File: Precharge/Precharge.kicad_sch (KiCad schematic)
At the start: 6 parts, among them J1 1053091202, J2 1053091203, J3 1053091202, K1 Relay_SPST-NO, K2 Relay_SPST-NO

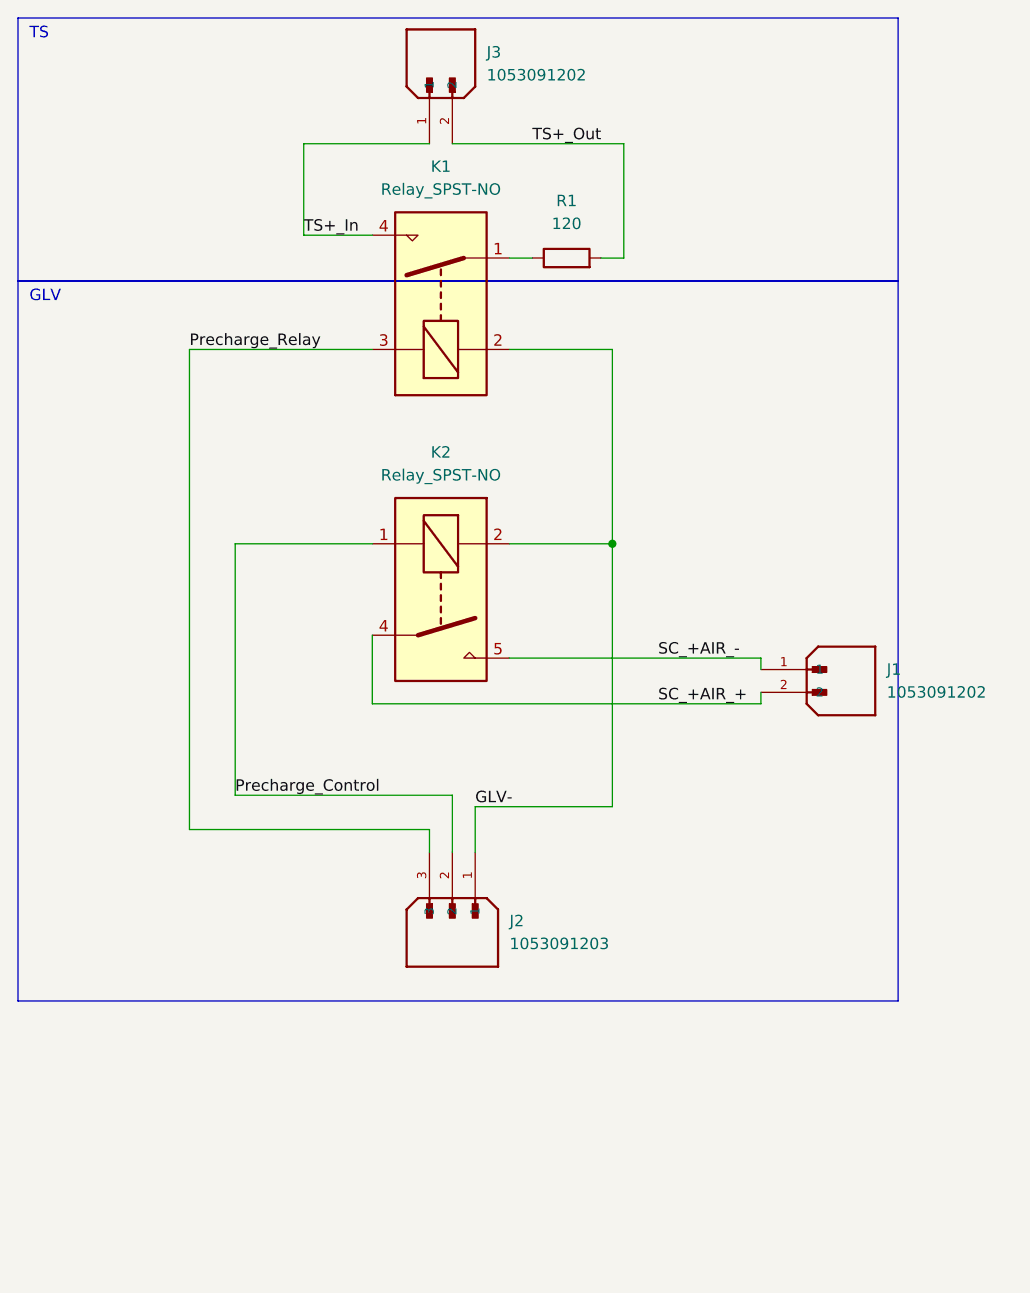
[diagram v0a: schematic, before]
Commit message: Added diodes to Precharge PCB
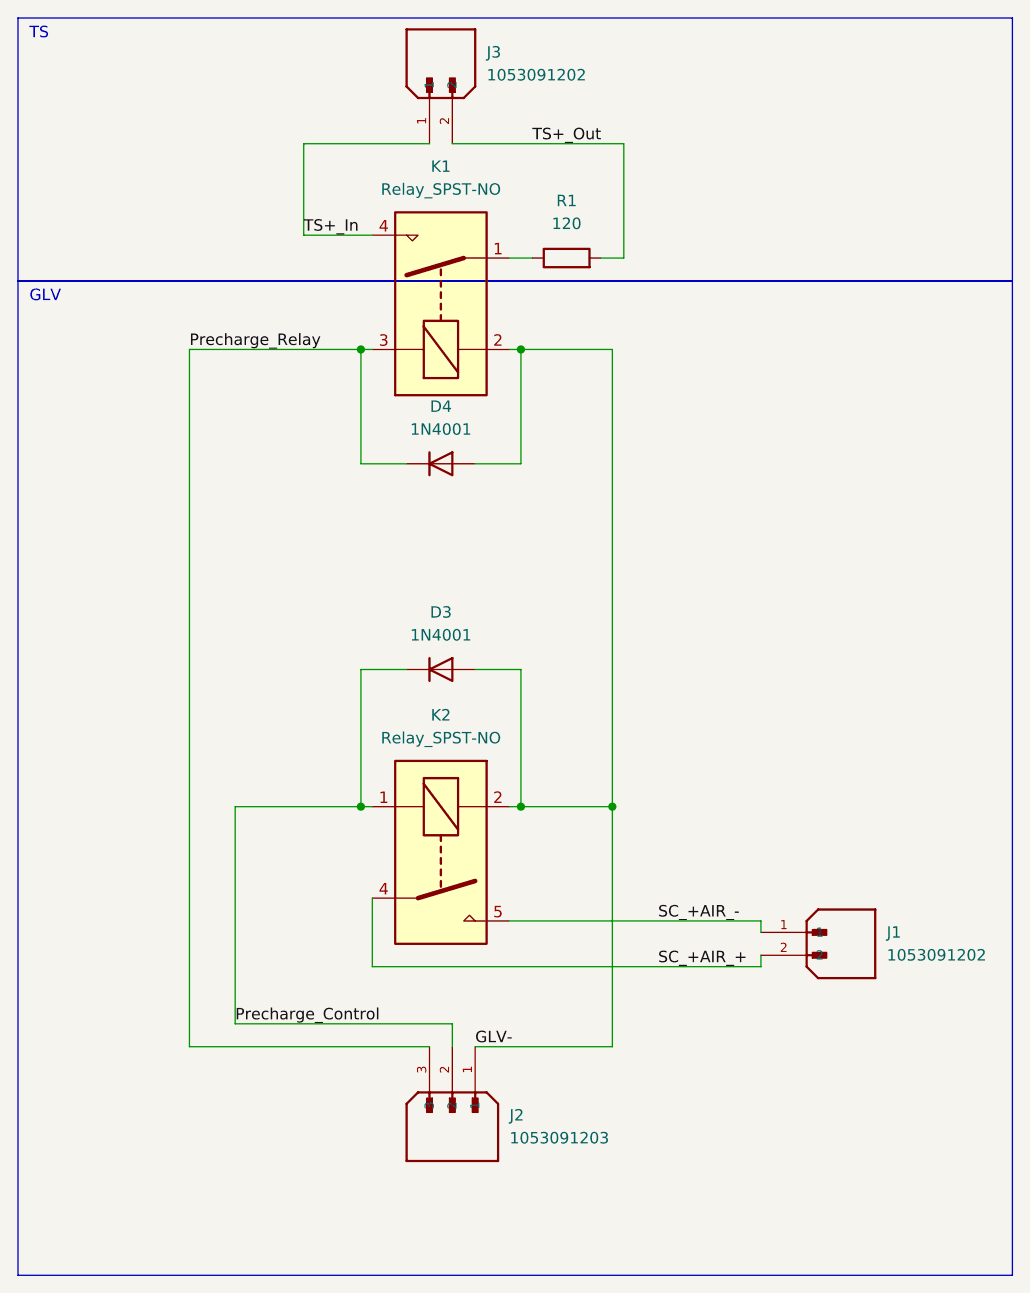
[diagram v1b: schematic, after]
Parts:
- added D3, D4: 1N4001, Diode_THT:D_DO-41_SOD81_P10.16mm_Horizontal, symbol Diode:1N4001
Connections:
- net GLV-: now also D3.2 (A), D4.2 (A)
- net Precharge_Control: now also D3.1 (K)
- net Precharge_Relay: now also D4.1 (K)
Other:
- moved on the sheet: J1, J2, K2

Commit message: Updated BSPD/Acc/PreCh to Global Lib + some Symbol
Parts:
- J1, J3: footprint Precharge_Library:MOLEX_1053091202 -> 1FS_2_Global_Footprint_Library:MOLEX_1053091202
- J2: footprint Precharge_Library:MOLEX_1053091203 -> 1FS_2_Global_Footprint_Library:MOLEX_1053091203
- K1: footprint Precharge_Library:G5PZ-1A-X DC12 -> 1FS_2_Global_Footprint_Library:G5PZ-1A-X DC12
- K2: footprint Precharge_Library:V23076A3001C132 -> 1FS_2_Global_Footprint_Library:V23076A3001C132
- R1: footprint Precharge_Library:THS15120RJ -> 1FS_2_Global_Footprint_Library:THS15120RJ
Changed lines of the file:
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@@
       (effects (font (size 1.27 1.27)) (justify right))
     )
-    (property "Footprint" "Precharge_Library:MOLEX_1053091202" (at 58.42 21.59 0)
+    (property "Footprint" "1FS_2_Global_Footprint_Library:MOLEX_1053091202" (at 58.42 21.59 0)
       (effects (font (size 1.27 1.27)) (justify bottom) hide)
     )
@@
       (effects (font (size 1.27 1.27)) (justify bottom) hide)
     )
-    (pin "2")
-    (pin "1")
+    (pin "1")
+    (pin "2")
     (instances
       (project "Precharge"
@@
       (effects (font (size 1.27 1.27)))
     )
-    (property "Footprint" "Precharge_Library:G5PZ-1A-X DC12" (at 60.96 33.02 0)
+    (property "Footprint" "1FS_2_Global_Footprint_Library:G5PZ-1A-X DC12" (at 60.96 33.02 0)
       (effects (font (size 1.27 1.27)) (justify left) hide)
     )
@@
       (effects (font (size 1.27 1.27)) hide)
     )
+    (pin "1")
+    (pin "2")
     (pin "3")
-    (pin "2")
     (pin "4")
-    (pin "1")
     (instances
       (project "Precharge"
@@
       (effects (font (size 1.27 1.27)) hide)
     )
-    (pin "2")
-    (pin "1")
+    (pin "1")
+    (pin "2")
     (instances
       (project "Precharge"
@@
       (effects (font (size 1.27 1.27)))
     )
-    (property "Footprint" "Precharge_Library:V23076A3001C132" (at 58.42 116.84 0)
+    (property "Footprint" "1FS_2_Global_Footprint_Library:V23076A3001C132" (at 58.42 116.84 0)
       (effects (font (size 1.27 1.27)) (justify left) hide)
     )
@@
       (effects (font (size 1.27 1.27)) hide)
     )
+    (pin "1")
+    (pin "2")
+    (pin "4")
     (pin "5")
-    (pin "1")
-    (pin "4")
-    (pin "2")
     (instances
       (project "Precharge"
@@
       (effects (font (size 1.27 1.27)) (justify left))
     )
-    (property "Footprint" "Precharge_Library:MOLEX_1053091203" (at 71.12 135.89 0)
+    (property "Footprint" "1FS_2_Global_Footprint_Library:MOLEX_1053091203" (at 71.12 135.89 0)
       (effects (font (size 1.27 1.27)) (justify bottom) hide)
     )
@@
       (effects (font (size 1.27 1.27)) hide)
     )
-    (pin "2")
-    (pin "1")
+    (pin "1")
+    (pin "2")
     (instances
       (project "Precharge"
@@
       (effects (font (size 1.27 1.27)))
     )
-    (property "Footprint" "Precharge_Library:THS15120RJ" (at 73.66 41.148 90)
+    (property "Footprint" "1FS_2_Global_Footprint_Library:THS15120RJ" (at 73.66 41.148 90)
       (effects (font (size 1.27 1.27)) hide)
     )
@@
       (effects (font (size 1.27 1.27)) hide)
     )
+    (pin "+")
     (pin "-")
-    (pin "+")
     (instances
       (project "Precharge"
@@
       (effects (font (size 1.27 1.27)) (justify left))
     )
-    (property "Footprint" "Precharge_Library:MOLEX_1053091202" (at 100.33 114.3 0)
+    (property "Footprint" "1FS_2_Global_Footprint_Library:MOLEX_1053091202" (at 100.33 114.3 0)
       (effects (font (size 1.27 1.27)) (justify bottom) hide)
     )
@@
       (effects (font (size 1.27 1.27)) (justify bottom) hide)
     )
-    (pin "2")
-    (pin "1")
-    (instances
-      (project "Precharge"
+    (pin "1")
+    (pin "2")
+    (instances
+      (project "Precharge"
